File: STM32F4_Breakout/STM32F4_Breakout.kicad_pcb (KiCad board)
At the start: 4 copper layers, 50 x 49.8 mm, 44 parts, among them J1 Conn_01x02, J2 Conn_01x02, J3 Conn_01x02, J4 Conn_02x05_Odd_Even, J5 Conn_01x04, J6 Conn_01x02, U1 AMS1117-3.3, U2 STM32F405RGT6

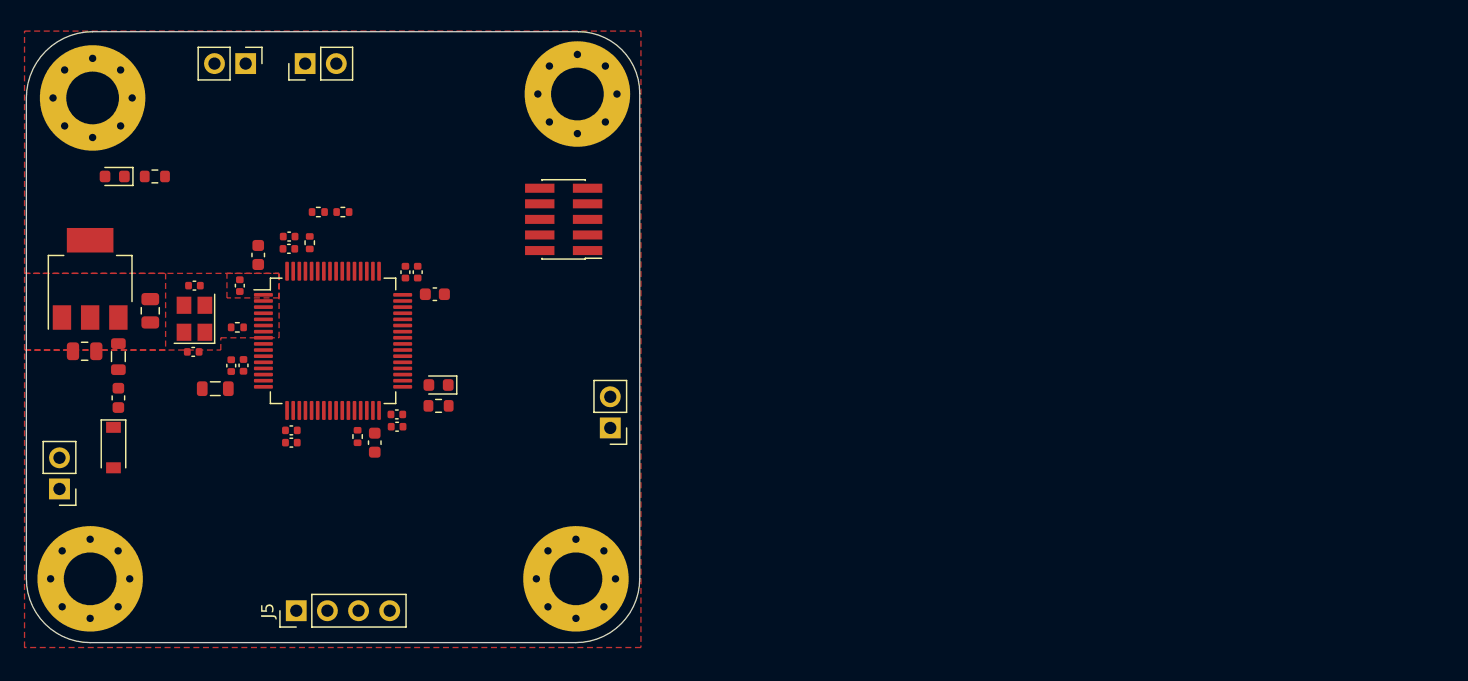
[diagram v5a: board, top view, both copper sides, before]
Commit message: fixing issue with the layer power plane assignment
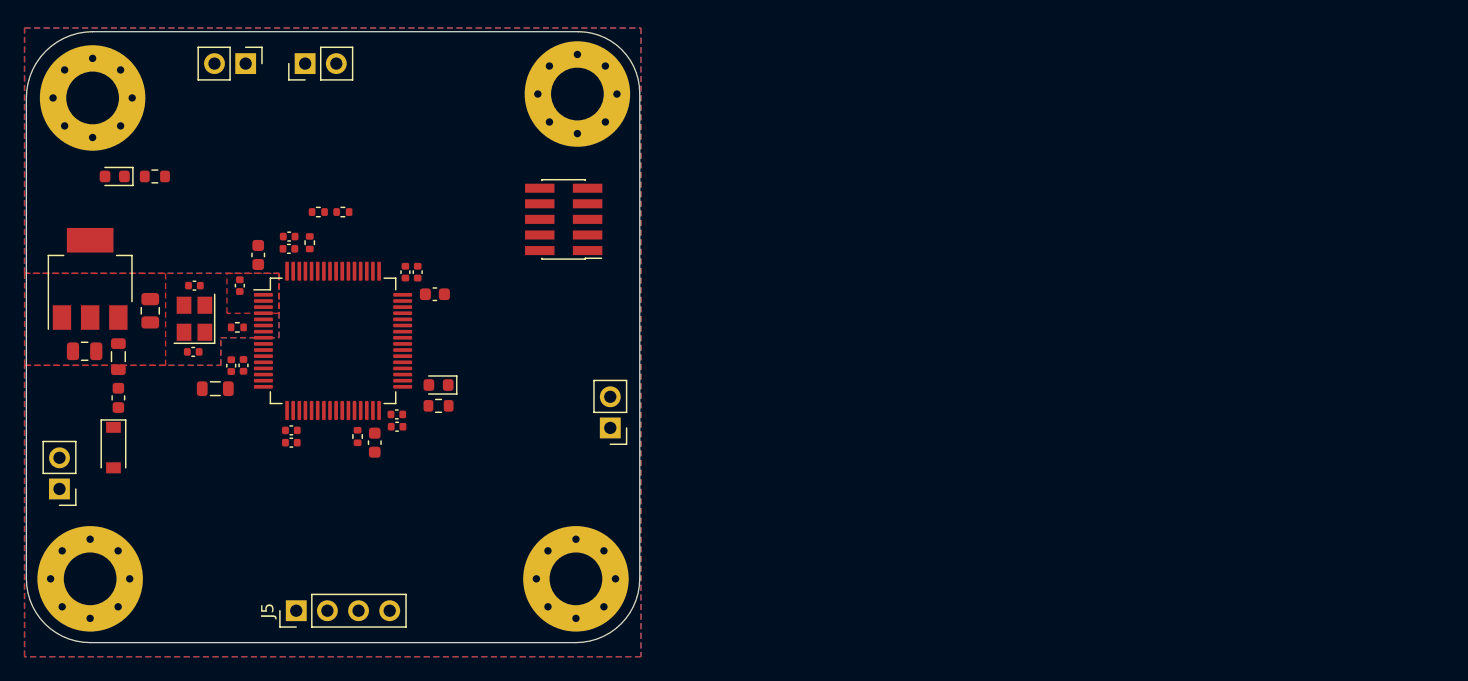
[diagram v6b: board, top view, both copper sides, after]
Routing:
- added copper zone on In2.Cu, net +3V3
- added copper zone on B.Cu, net GND
- added copper zone on In1.Cu, net GND
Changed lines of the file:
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@@
     (polygon
       (pts
-        (xy 81 61.5)
-        (xy 76.75 61.5)
+        (xy 81 62.75)
+        (xy 76.75 62.75)
         (xy 76.75 59.5)
         (xy 81 59.5)
@@
     (polygon
       (pts
-        (xy 71.75 65.75)
-        (xy 60.25 65.75)
+        (xy 71.75 67)
+        (xy 60.25 67)
         (xy 60.25 59.5)
         (xy 71.75 59.5)
@@
     (polygon
       (pts
-        (xy 110.5 90)
-        (xy 60.25 90)
-        (xy 60.25 65.75)
-        (xy 76.25 65.75)
+        (xy 110.5 90.75)
+        (xy 60.25 90.75)
+        (xy 60.25 67)
+        (xy 76.25 67)
         (xy 76.25 64.75)
         (xy 81 64.75)
         (xy 81 59.5)
         (xy 60.25 59.5)
-        (xy 60.25 39.75)
-        (xy 110.5 39.75)
+        (xy 60.25 39.5)
+        (xy 110.5 39.5)
       )
     )
+  )
+  (zone (net 1) (net_name "GND") (layer "In1.Cu") (hatch edge 0.508)
+    (connect_pads (clearance 0.508))
+    (min_thickness 0.254) (filled_areas_thickness no)
+    (fill yes (thermal_gap 0.508) (thermal_bridge_width 0.508))
+    (polygon
+      (pts
+        (xy 110.5 90.75)
+        (xy 60.25 90.75)
+        (xy 60.25 67)
+        (xy 76.25 67)
+        (xy 76.25 64.75)
+        (xy 81 64.75)
+        (xy 81 59.5)
+        (xy 60.25 59.5)
+        (xy 60.25 39.5)
+        (xy 110.5 39.5)
+      )
+    )
+  )
+  (zone (net 9) (net_name "+3V3") (layer "In2.Cu") (hatch edge 0.508)
+    (connect_pads (clearance 0.508))
+    (min_thickness 0.254) (filled_areas_thickness no)
+    (fill yes (thermal_gap 0.508) (thermal_bridge_width 0.508))
+    (polygon
+      (pts
+        (xy 110.5 90.75)
+        (xy 60.25 90.75)
+        (xy 60.25 67)
+        (xy 76.25 67)
+        (xy 76.25 64.75)
+        (xy 81 64.75)
+        (xy 81 59.5)
+        (xy 60.25 59.5)
+        (xy 60.25 39.5)
+        (xy 110.5 39.5)
+      )
+    )
+  )
+  (zone (net 1) (net_name "GND") (layer "B.Cu") (hatch edge 0.508)
+    (connect_pads (clearance 0.508))
+    (min_thickness 0.254) (filled_areas_thickness no)
+    (fill yes (thermal_gap 0.508) (thermal_bridge_width 0.508))
+    (polygon
+      (pts
+        (xy 110.5 90.75)
+        (xy 60.25 90.75)
+        (xy 60.25 67)
+        (xy 76.25 67)
+        (xy 76.25 64.75)
+        (xy 81 64.75)
+        (xy 81 59.5)
+        (xy 60.25 59.5)
+        (xy 60.25 39.5)
+        (xy 110.5 39.5)
+      )
+    )

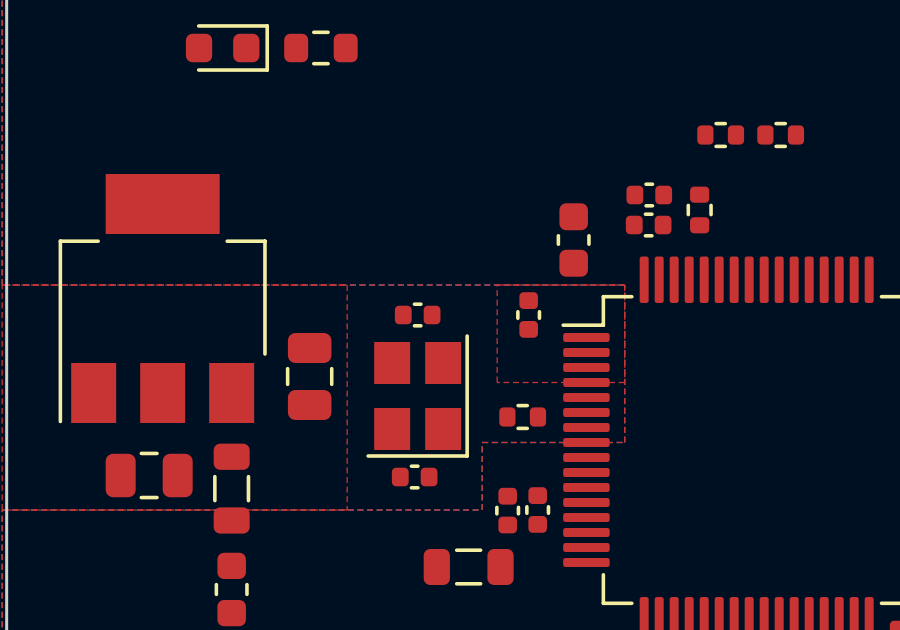
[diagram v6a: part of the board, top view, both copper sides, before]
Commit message: fixing copper ours and gnd polygon around crystal
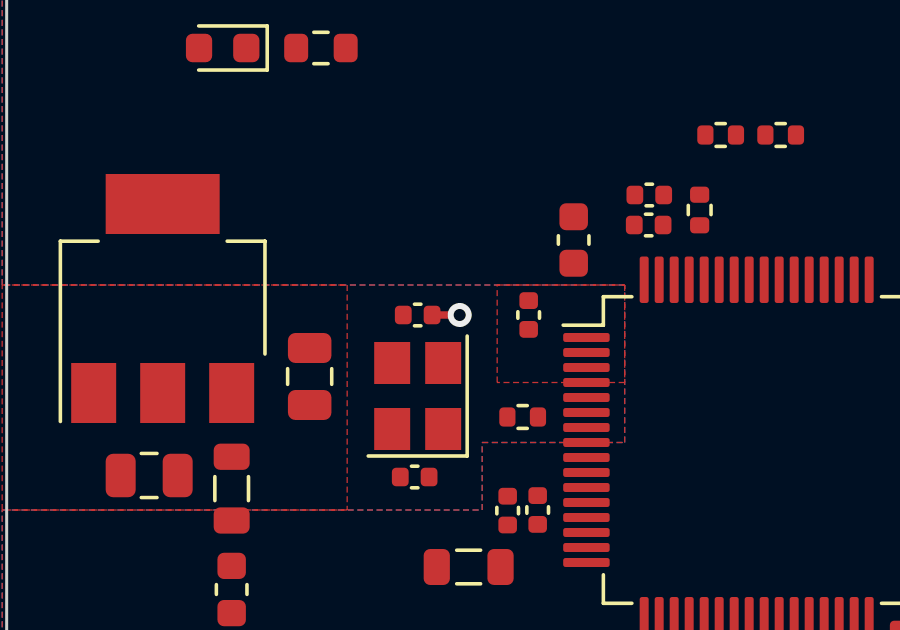
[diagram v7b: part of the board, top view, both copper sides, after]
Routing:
- net GND: track 0.00 -> 0.92 mm, vias 0 -> 1
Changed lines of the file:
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@@
   (gr_arc (start 110.4 84.4) (mid 108.876955 88.076955) (end 105.2 89.6) (layer "Edge.Cuts") (width 0.1))
   (gr_arc (start 60.4 45.2) (mid 61.981623 41.381623) (end 65.8 39.8) (layer "Edge.Cuts") (width 0.1))
+  (segment (start 74.58 60.5) (end 75.5 60.5) (width 0.25) (layer "F.Cu") (net 1))
+  (via (at 75.5 60.5) (size 0.8) (drill 0.4) (layers "F.Cu" "B.Cu") (free) (net 1))
   (zone (net 1) (net_name "GND") (layer "F.Cu") (hatch edge 0.508)
     (connect_pads (clearance 0.508))
@@
       )
     )
+  )
+  (zone (net 1) (net_name "GND") (layer "In1.Cu") (hatch edge 0.508)
+    (connect_pads (clearance 0.508))
+    (min_thickness 0.254) (filled_areas_thickness no)
+    (fill yes (thermal_gap 0.508) (thermal_bridge_width 0.508))
+    (polygon
+      (pts
+        (xy 75.9 61)
+        (xy 75.9 61)
+        (xy 75.9 63.4)
+        (xy 78.9 63.4)
+        (xy 78.9 63.2)
+        (xy 80.4 63.2)
+        (xy 80.4 63.8)
+        (xy 78.5 63.8)
+        (xy 78.5 64.4)
+        (xy 75.9 64.4)
+        (xy 75.9 65.4)
+        (xy 75.9 65.4)
+        (xy 75.9 66.4)
+        (xy 72.4 66.4)
+        (xy 72.4 61)
+        (xy 72.4 61)
+        (xy 72.4 60)
+        (xy 75.9 60)
+      )
+    )

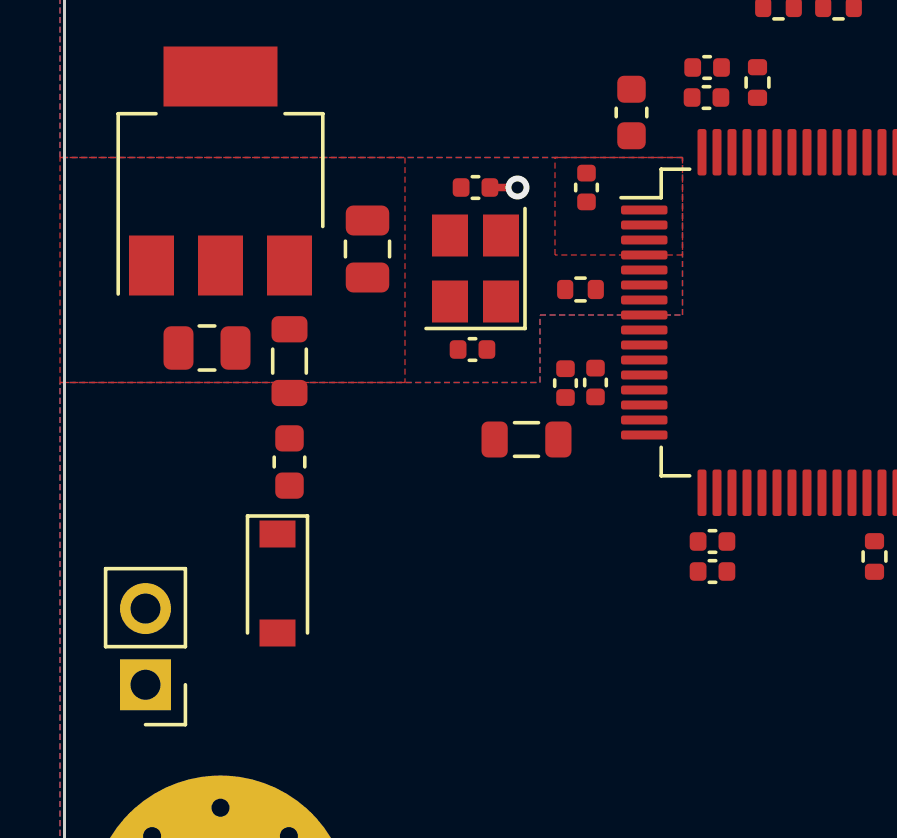
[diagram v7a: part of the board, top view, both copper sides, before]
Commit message: routing crystal oscillator per datasheet
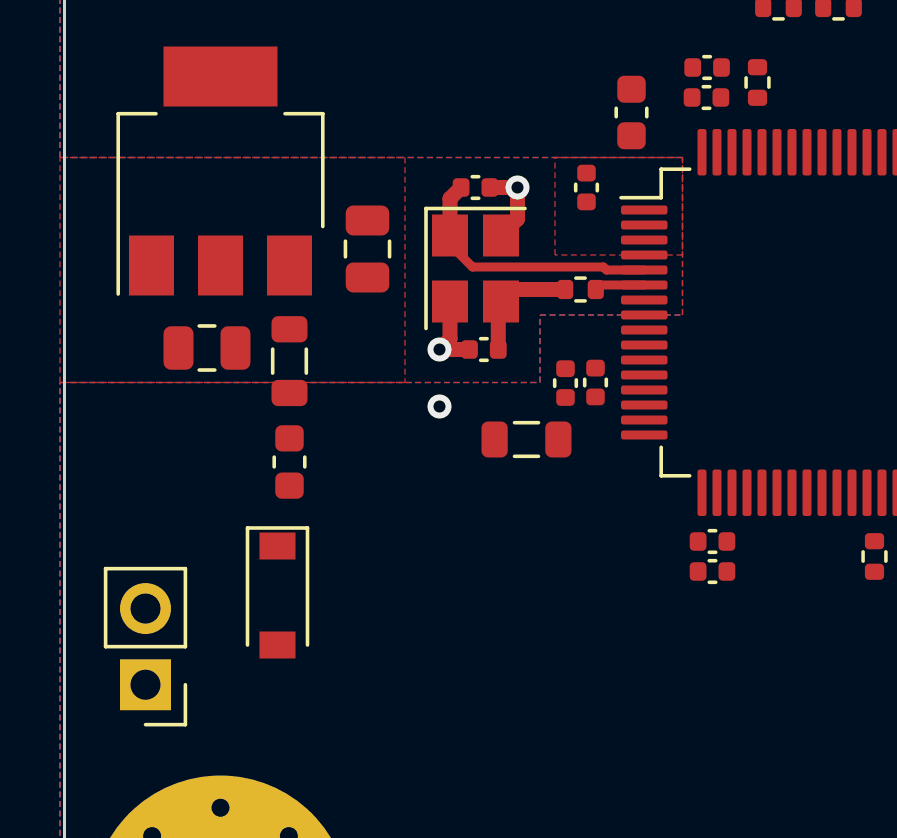
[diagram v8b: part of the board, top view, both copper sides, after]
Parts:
- moved D1 0.40 mm to (67.5, 74.1)
- moved C18 0.38 mm to (74.4, 65.9), turned to 180 degrees
- turned HSE1 to -90 degrees
- turned R6 to 0 degrees
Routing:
- net HSE_IN: track 0.00 -> 8.88 mm
- net GND: track 0.92 -> 7.39 mm, vias 1 -> 3
- net Net-(C18-Pad1): track 0.00 -> 3.94 mm
- net HSE_OUT: track 0.00 -> 1.68 mm
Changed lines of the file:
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@@
   )
   (footprint "Resistor_SMD:R_0402_1005Metric" (layer "F.Cu")
-    (at 77.6 63.9 180)
+    (at 77.6 63.9)
     (descr "Resistor SMD 0402 (1005 Metric), square (rectangular) end terminal, IPC_7351 nominal, (Body size source: IPC-SM-782 page 72, https://www.pcb-3d.com/wordpress/wp-content/uploads/ipc-sm-782a_amendment_1_and_2.pdf), generated with kicad-footprint-generator")
     (tags "resistor")
@@
     (fp_line (start 0.525 -0.27) (end 0.525 0.27) (layer "F.Fab") (width 0.1))
     (fp_line (start -0.525 0.27) (end -0.525 -0.27) (layer "F.Fab") (width 0.1))
-    (pad "1" smd roundrect (at -0.51 0 180) (size 0.54 0.64) (layers "F.Cu" "F.Paste" "F.Mask") (roundrect_rratio 0.25)
+    (pad "1" smd roundrect (at -0.51 0) (size 0.54 0.64) (layers "F.Cu" "F.Paste" "F.Mask") (roundrect_rratio 0.25)
       (net 5 "Net-(C18-Pad1)") (pintype "passive"))
-    (pad "2" smd roundrect (at 0.51 0 180) (size 0.54 0.64) (layers "F.Cu" "F.Paste" "F.Mask") (roundrect_rratio 0.25)
+    (pad "2" smd roundrect (at 0.51 0) (size 0.54 0.64) (layers "F.Cu" "F.Paste" "F.Mask") (roundrect_rratio 0.25)
       (net 6 "HSE_OUT") (pintype "passive"))
     (model "${KICAD6_3DMODEL_DIR}/Resistor_SMD.3dshapes/R_0402_1005Metric.wrl"
@@
   )
   (footprint "Diode_SMD:D_SOD-123" (layer "F.Cu")
-    (at 67.5 73.7 -90)
+    (at 67.5 74.1 -90)
     (descr "SOD-123")
     (tags "SOD-123")
@@
   )
   (footprint "Crystal:Crystal_SMD_3225-4Pin_3.2x2.5mm" (layer "F.Cu")
-    (at 74.1 63.2 90)
+    (at 74.1 63.2 -90)
     (descr "SMD Crystal SERIES SMD3225/4 http://www.txccrystal.com/images/pdf/7m-accuracy.pdf, 3.2x2.5mm^2 package")
     (tags "SMD SMT crystal")
@@
     (fp_line (start -1.6 -1.25) (end -1.6 1.25) (layer "F.Fab") (width 0.1))
     (fp_line (start -1.6 0.25) (end -0.6 1.25) (layer "F.Fab") (width 0.1))
-    (pad "1" smd rect (at -1.1 0.85 90) (size 1.4 1.2) (layers "F.Cu" "F.Paste" "F.Mask")
+    (pad "1" smd rect (at -1.1 0.85 270) (size 1.4 1.2) (layers "F.Cu" "F.Paste" "F.Mask")
       (net 15 "HSE_IN") (pinfunction "1") (pintype "passive"))
-    (pad "2" smd rect (at 1.1 0.85 90) (size 1.4 1.2) (layers "F.Cu" "F.Paste" "F.Mask")
+    (pad "2" smd rect (at 1.1 0.85 270) (size 1.4 1.2) (layers "F.Cu" "F.Paste" "F.Mask")
       (net 1 "GND") (pinfunction "2") (pintype "passive"))
-    (pad "3" smd rect (at 1.1 -0.85 90) (size 1.4 1.2) (layers "F.Cu" "F.Paste" "F.Mask")
+    (pad "3" smd rect (at 1.1 -0.85 270) (size 1.4 1.2) (layers "F.Cu" "F.Paste" "F.Mask")
       (net 5 "Net-(C18-Pad1)") (pinfunction "3") (pintype "passive"))
-    (pad "4" smd rect (at -1.1 -0.85 90) (size 1.4 1.2) (layers "F.Cu" "F.Paste" "F.Mask")
+    (pad "4" smd rect (at -1.1 -0.85 270) (size 1.4 1.2) (layers "F.Cu" "F.Paste" "F.Mask")
       (net 1 "GND") (pinfunction "4") (pintype "passive"))
     (model "${KICAD6_3DMODEL_DIR}/Crystal.3dshapes/Crystal_SMD_3225-4Pin_3.2x2.5mm.wrl"
@@
   )
   (footprint "Capacitor_SMD:C_0402_1005Metric" (layer "F.Cu")
-    (at 74 65.9)
+    (at 74.38 65.9 180)
     (descr "Capacitor SMD 0402 (1005 Metric), square (rectangular) end terminal, IPC_7351 nominal, (Body size source: IPC-SM-782 page 76, https://www.pcb-3d.com/wordpress/wp-content/uploads/ipc-sm-782a_amendment_1_and_2.pdf), generated with kicad-footprint-generator")
     (tags "capacitor")
@@
     (fp_line (start 0.5 -0.25) (end 0.5 0.25) (layer "F.Fab") (width 0.1))
     (fp_line (start -0.5 -0.25) (end 0.5 -0.25) (layer "F.Fab") (width 0.1))
-    (pad "1" smd roundrect (at -0.48 0) (size 0.56 0.62) (layers "F.Cu" "F.Paste" "F.Mask") (roundrect_rratio 0.25)
+    (pad "1" smd roundrect (at -0.48 0 180) (size 0.56 0.62) (layers "F.Cu" "F.Paste" "F.Mask") (roundrect_rratio 0.25)
       (net 5 "Net-(C18-Pad1)") (pintype "passive"))
-    (pad "2" smd roundrect (at 0.48 0) (size 0.56 0.62) (layers "F.Cu" "F.Paste" "F.Mask") (roundrect_rratio 0.25)
+    (pad "2" smd roundrect (at 0.48 0 180) (size 0.56 0.62) (layers "F.Cu" "F.Paste" "F.Mask") (roundrect_rratio 0.25)
       (net 1 "GND") (pintype "passive"))
     (model "${KICAD6_3DMODEL_DIR}/Capacitor_SMD.3dshapes/C_0402_1005Metric.wrl"
@@
   (gr_arc (start 110.4 84.4) (mid 108.876955 88.076955) (end 105.2 89.6) (layer "Edge.Cuts") (width 0.1))
   (gr_arc (start 60.4 45.2) (mid 61.981623 41.381623) (end 65.8 39.8) (layer "Edge.Cuts") (width 0.1))
-  (segment (start 74.58 60.5) (end 75.5 60.5) (width 0.25) (layer "F.Cu") (net 1))
+  (segment (start 73.25 65.55) (end 72.9 65.9) (width 0.5) (layer "F.Cu") (net 1))
+  (segment (start 75.5 60.5) (end 75.5 61.55) (width 0.5) (layer "F.Cu") (net 1))
+  (segment (start 75.5 61.55) (end 74.95 62.1) (width 0.5) (layer "F.Cu") (net 1))
+  (segment (start 73.25 64.3) (end 73.25 65.55) (width 0.5) (layer "F.Cu") (net 1))
+  (segment (start 72.9 65.9) (end 73.9 65.9) (width 0.5) (layer "F.Cu") (net 1))
+  (segment (start 74.58 60.5) (end 75.5 60.5) (width 0.5) (layer "F.Cu") (net 1))
+  (via (at 72.9 65.9) (size 0.8) (drill 0.4) (layers "F.Cu" "B.Cu") (free) (net 1))
+  (via (at 72.9 67.8) (size 0.8) (drill 0.4) (layers "F.Cu" "B.Cu") (net 1))
   (via (at 75.5 60.5) (size 0.8) (drill 0.4) (layers "F.Cu" "B.Cu") (free) (net 1))
+  (segment (start 72.9 67.8) (end 72.9 65.9) (width 0.5) (layer "In1.Cu") (net 1))
+  (segment (start 74.86 64.39) (end 74.95 64.3) (width 0.5) (layer "F.Cu") (net 5))
+  (segment (start 75.35 63.9) (end 74.95 64.3) (width 0.5) (layer "F.Cu") (net 5))
+  (segment (start 77.09 63.9) (end 75.35 63.9) (width 0.5) (layer "F.Cu") (net 5))
+  (segment (start 74.86 65.9) (end 74.86 64.39) (width 0.5) (layer "F.Cu") (net 5))
+  (segment (start 78.26 63.75) (end 79.725 63.75) (width 0.3) (layer "F.Cu") (net 6))
+  (segment (start 78.11 63.9) (end 78.26 63.75) (width 0.3) (layer "F.Cu") (net 6))
+  (segment (start 73.25 62.4) (end 73.25 62.1) (width 0.3) (layer "F.Cu") (net 15))
+  (segment (start 78.365894 63.15) (end 74 63.15) (width 0.3) (layer "F.Cu") (net 15))
+  (segment (start 73.25 62.1) (end 73.25 60.87) (width 0.5) (layer "F.Cu") (net 15))
+  (segment (start 78.465894 63.25) (end 78.365894 63.15) (width 0.3) (layer "F.Cu") (net 15))
+  (segment (start 74 63.15) (end 73.25 62.4) (width 0.3) (layer "F.Cu") (net 15))
+  (segment (start 79.725 63.25) (end 78.465894 63.25) (width 0.3) (layer "F.Cu") (net 15))
+  (segment (start 73.25 60.87) (end 73.62 60.5) (width 0.5) (layer "F.Cu") (net 15))
   (zone (net 1) (net_name "GND") (layer "F.Cu") (hatch edge 0.508)
     (connect_pads (clearance 0.508))
@@
       (pts
         (xy 75.9 61)
-        (xy 75.9 61)
         (xy 75.9 63.4)
         (xy 78.9 63.4)
@@
         (xy 75.9 64.4)
         (xy 75.9 65.4)
-        (xy 75.9 65.4)
         (xy 75.9 66.4)
         (xy 72.4 66.4)
         (xy 72.4 61)
-        (xy 72.4 61)
         (xy 72.4 60)
